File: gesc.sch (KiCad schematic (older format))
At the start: 34 parts, among them J1 Conn_01x06, J13 T-Motor, J15 EXT_OFF, J2 Conn_01x06, J3 Conn_01x06, J4 Conn_01x05, J5 Conn_01x03, J6 USB_B_Mini, J7 BAT+, J8 BAT-

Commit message: save
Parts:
- J7, J8: footprint gsvesc:TestPoint_Pad_5.0x5.0mm -> gesc:TestPoint_Pad_5.0x5.0mm
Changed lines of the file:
@@
 encoding utf-8
 Sheet 1 5
-Title "GSESC - DC Motor Controler"
+Title "GESC - DC Motor Controler"
 Date "2020-04-09"
-Rev "4.0"
+Rev "6.0"
 Comp ""
 Comment1 ""
@@
 U 5BECFBE3
 F0 "NRF" 50
-F1 "gsvesc_nrf.sch" 50
+F1 "gesc_nrf.sch" 50
 F2 "NRF_TX" I L 5200 5300 50
 F3 "NRF_RX" I L 5200 5400 50
@@
 F 0 "J7" H 10930 1392 50  0000 L CNN
 F 1 "BAT+" H 10930 1301 50  0000 L CNN
-F 2 "gsvesc:TestPoint_Pad_5.0x5.0mm" H 10850 1350 50  0001 C CNN
+F 2 "gesc:TestPoint_Pad_5.0x5.0mm" H 10850 1350 50  0001 C CNN
 F 3 "~" H 10850 1350 50  0001 C CNN
 	1    10850 1350
@@
 F 0 "J8" H 10930 1942 50  0000 L CNN
 F 1 "BAT-" H 10930 1851 50  0000 L CNN
-F 2 "gsvesc:TestPoint_Pad_5.0x5.0mm" H 10850 1900 50  0001 C CNN
+F 2 "gesc:TestPoint_Pad_5.0x5.0mm" H 10850 1900 50  0001 C CNN
 F 3 "~" H 10850 1900 50  0001 C CNN
 	1    10850 1900
@@
 U 5BE81C34
 F0 "MCU" 50
-F1 "gsvesc_uc.sch" 50
+F1 "gesc_uc.sch" 50
 F2 "USB_D+" B L 3250 1700 50
 F3 "USB_D-" B L 3250 1800 50
@@
 U 5BECFABD
 F0 "POWER" 50
-F1 "gsvesc_pwr.sch" 50
+F1 "gesc_pwr.sch" 50
 F2 "GH_A" I L 7550 2050 50
 F3 "SH_A" I L 7550 2150 50

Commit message: save
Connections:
- net VBUS: now reaches J6.1 (VBUS)
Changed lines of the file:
@@
 	2400 5750 2550 5750
 Connection ~ 2550 5750
+Wire Wire Line
+	1900 1500 2100 1500
+$Comp
+L power:PWR_FLAG #FLG0106
+U 1 1 60156C51
+P 9550 3100
+F 0 "#FLG0106" H 9550 3175 50  0001 C CNN
+F 1 "PWR_FLAG" V 9550 3228 50  0000 L CNN
+F 2 "" H 9550 3100 50  0001 C CNN
+F 3 "~" H 9550 3100 50  0001 C CNN
+	1    9550 3100
+	0    -1   -1   0
+$EndComp
+Wire Wire Line
+	9550 3100 9950 3100
+$Comp
+L power:VBUS #PWR0149
+U 1 1 6015CFC2
+P 9950 3100
+F 0 "#PWR0149" H 9950 2950 50  0001 C CNN
+F 1 "VBUS" V 9965 3228 50  0000 L CNN
+F 2 "" H 9950 3100 50  0001 C CNN
+F 3 "" H 9950 3100 50  0001 C CNN
+	1    9950 3100
+	0    1    1    0
+$EndComp
+$Comp
+L power:VBUS #PWR0150
+U 1 1 6015E336
+P 2100 1500
+F 0 "#PWR0150" H 2100 1350 50  0001 C CNN
+F 1 "VBUS" V 2115 1628 50  0000 L CNN
+F 2 "" H 2100 1500 50  0001 C CNN
+F 3 "" H 2100 1500 50  0001 C CNN
+	1    2100 1500
+	0    1    1    0
+$EndComp
 $EndSCHEMATC

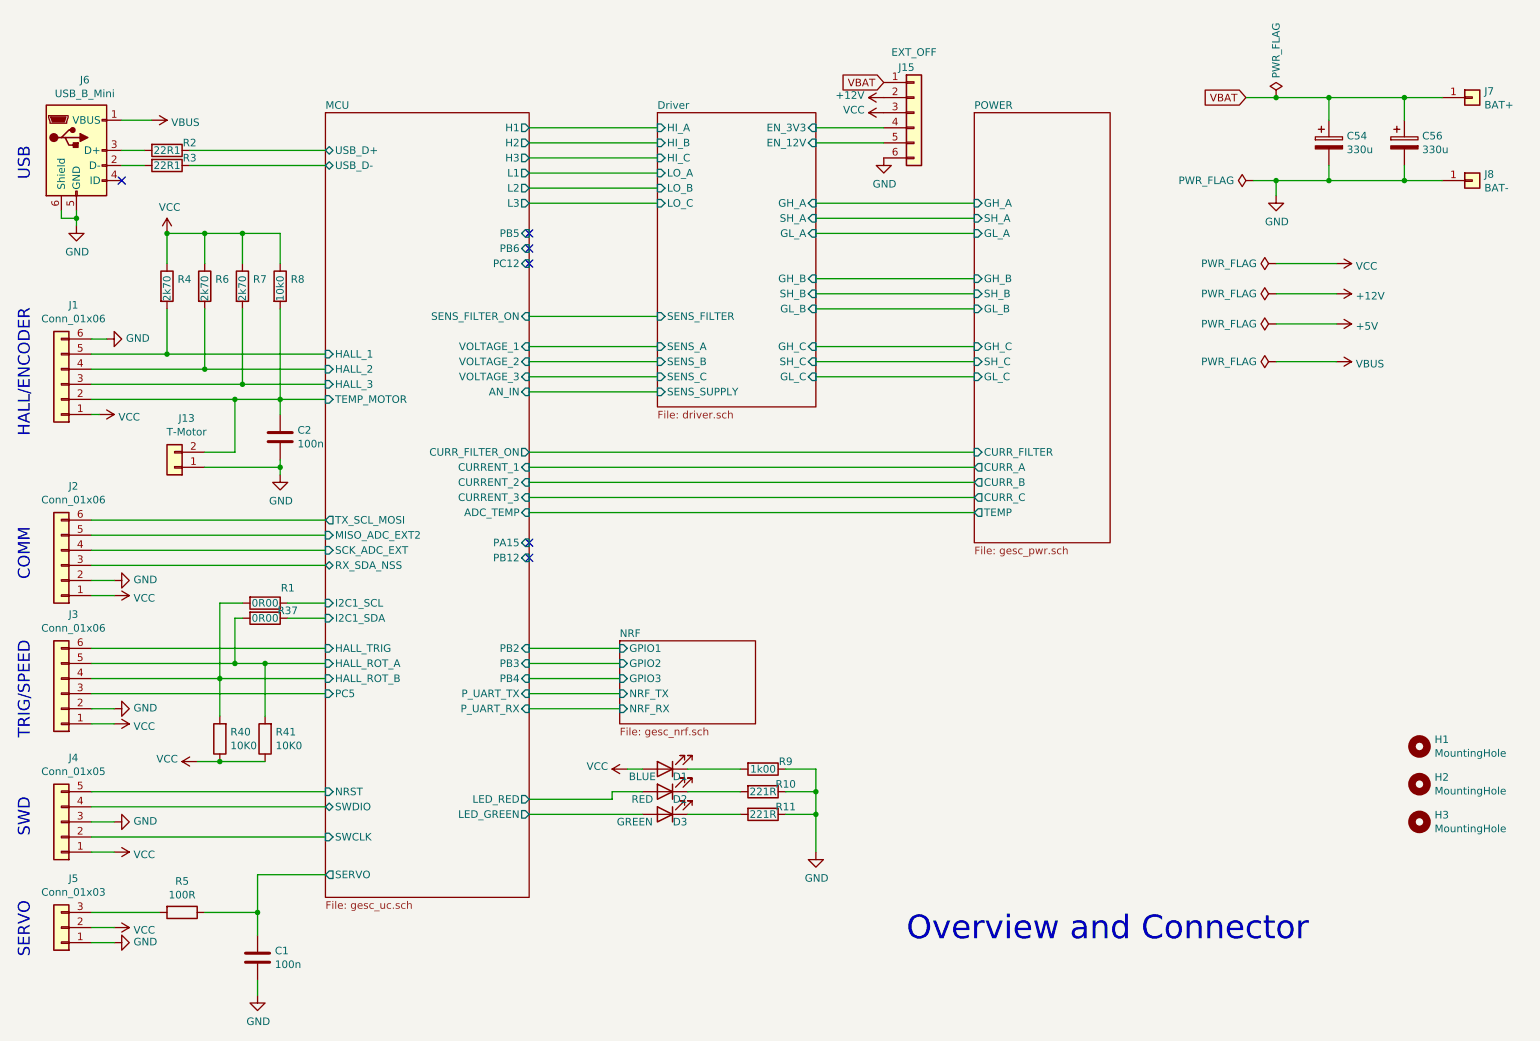
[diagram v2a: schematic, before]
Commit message: - remove solder-mask from bottom layer
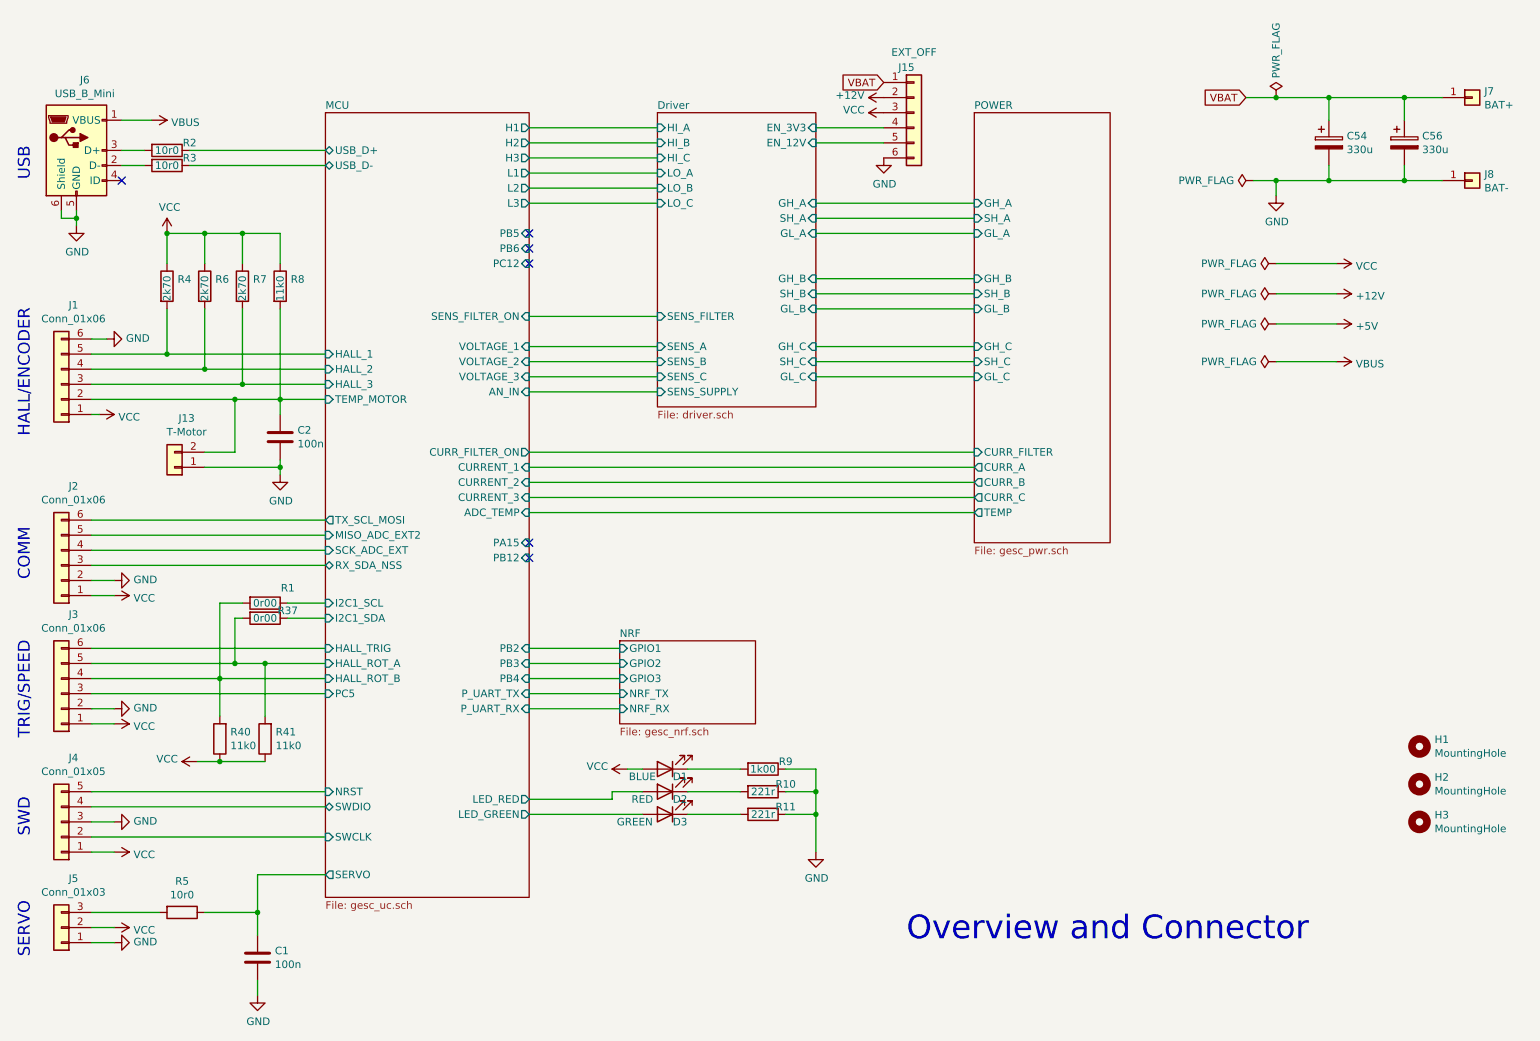
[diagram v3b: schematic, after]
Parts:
- R1, R37: value 0R00 -> 0r00
- R10, R11: value 221R -> 221r
- R2, R3: value 22R1 -> 10r0
- R40, R41: value 10K0 -> 11k0
- R5: value 100R -> 10r0
- R8: value 10k0 -> 11k0
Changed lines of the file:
@@
 P 2200 1700
 F 0 "R2" V 2150 1850 50  0000 C CNN
-F 1 "22R1" V 2200 1700 50  0000 C CNN
+F 1 "10r0" V 2200 1700 50  0000 C CNN
 F 2 "Resistor_SMD:R_0805_2012Metric" V 2130 1700 50  0001 C CNN
 F 3 "~" H 2200 1700 50  0001 C CNN
@@
 P 2200 1800
 F 0 "R3" V 2150 1950 50  0000 C CNN
-F 1 "22R1" V 2200 1800 50  0000 C CNN
+F 1 "10r0" V 2200 1800 50  0000 C CNN
 F 2 "Resistor_SMD:R_0805_2012Metric" V 2130 1800 50  0001 C CNN
 F 3 "~" H 2200 1800 50  0001 C CNN
@@
 P 2950 2600
 F 0 "R8" H 3020 2646 50  0000 L CNN
-F 1 "10k0" V 2950 2500 50  0000 L CNN
+F 1 "11k0" V 2950 2500 50  0000 L CNN
 F 2 "Resistor_SMD:R_0805_2012Metric" V 2880 2600 50  0001 C CNN
 F 3 "~" H 2950 2600 50  0001 C CNN
@@
 P 2300 6750
 F 0 "R5" V 2093 6750 50  0000 C CNN
-F 1 "100R" V 2184 6750 50  0000 C CNN
+F 1 "10r0" V 2184 6750 50  0000 C CNN
 F 2 "Resistor_SMD:R_0805_2012Metric" V 2230 6750 50  0001 C CNN
 F 3 "~" H 2300 6750 50  0001 C CNN
@@
 P 6150 5950
 F 0 "R10" V 6100 6100 50  0000 C CNN
-F 1 "221R" V 6150 5950 50  0000 C CNN
+F 1 "221r" V 6150 5950 50  0000 C CNN
 F 2 "Resistor_SMD:R_0805_2012Metric" V 6080 5950 50  0001 C CNN
 F 3 "~" H 6150 5950 50  0001 C CNN
@@
 P 6150 6100
 F 0 "R11" V 6100 6250 50  0000 C CNN
-F 1 "221R" V 6150 6100 50  0000 C CNN
+F 1 "221r" V 6150 6100 50  0000 C CNN
 F 2 "Resistor_SMD:R_0805_2012Metric" V 6080 6100 50  0001 C CNN
 F 3 "~" H 6150 6100 50  0001 C CNN
@@
 Wire Wire Line
 	10400 1900 10650 1900
-$Comp
-L Device:R R1
-U 1 1 5F2F9B0D
-P 2850 4700
-F 0 "R1" V 2750 4850 50  0000 C CNN
-F 1 "0R00" V 2850 4700 50  0000 C CNN
-F 2 "Resistor_SMD:R_0805_2012Metric" V 2780 4700 50  0001 C CNN
-F 3 "~" H 2850 4700 50  0001 C CNN
-	1    2850 4700
-	0    1    1    0
-$EndComp
-$Comp
-L Device:R R37
-U 1 1 5F2F9BE2
-P 2850 4800
-F 0 "R37" V 2800 4950 50  0000 C CNN
-F 1 "0R00" V 2850 4800 50  0000 C CNN
-F 2 "Resistor_SMD:R_0805_2012Metric" V 2780 4800 50  0001 C CNN
-F 3 "~" H 2850 4800 50  0001 C CNN
-	1    2850 4800
-	0    1    1    0
-$EndComp
 Wire Wire Line
 	3250 4700 3000 4700
@@
 P 2550 5600
 F 0 "R40" H 2480 5554 50  0000 R CNN
-F 1 "10K0" H 2480 5645 50  0000 R CNN
+F 1 "11k0" H 2480 5645 50  0000 R CNN
 F 2 "Resistor_SMD:R_0805_2012Metric" V 2480 5600 50  0001 C CNN
 F 3 "~" H 2550 5600 50  0001 C CNN
@@
 P 2850 5600
 F 0 "R41" H 2780 5554 50  0000 R CNN
-F 1 "10K0" H 2780 5645 50  0000 R CNN
+F 1 "11k0" H 2780 5645 50  0000 R CNN
 F 2 "Resistor_SMD:R_0805_2012Metric" V 2780 5600 50  0001 C CNN
 F 3 "~" H 2850 5600 50  0001 C CNN
@@
 	0    1    1    0
 $EndComp
+$Comp
+L Device:R R37
+U 1 1 5F2F9BE2
+P 2850 4800
+F 0 "R37" V 2800 4950 50  0000 C CNN
+F 1 "0r00" V 2850 4800 50  0000 C CNN
+F 2 "Resistor_SMD:R_0805_2012Metric" V 2780 4800 50  0001 C CNN
+F 3 "~" H 2850 4800 50  0001 C CNN
+	1    2850 4800
+	0    1    1    0
+$EndComp
+$Comp
+L Device:R R1
+U 1 1 5F2F9B0D
+P 2850 4700
+F 0 "R1" V 2750 4850 50  0000 C CNN
+F 1 "0r00" V 2850 4700 50  0000 C CNN
+F 2 "Resistor_SMD:R_0805_2012Metric" V 2780 4700 50  0001 C CNN
+F 3 "~" H 2850 4700 50  0001 C CNN
+	1    2850 4700
+	0    1    1    0
+$EndComp
